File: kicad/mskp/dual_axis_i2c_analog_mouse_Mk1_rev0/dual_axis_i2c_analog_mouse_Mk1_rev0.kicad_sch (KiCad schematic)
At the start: 16 parts, among them J1 I2C_input_controller_JST, J2 I2C_input_controller_pads, J3 mouse_input_pads, J4 mouse_input_JST, U1 ADS1113IDGS, U2 AMS1117-3.3

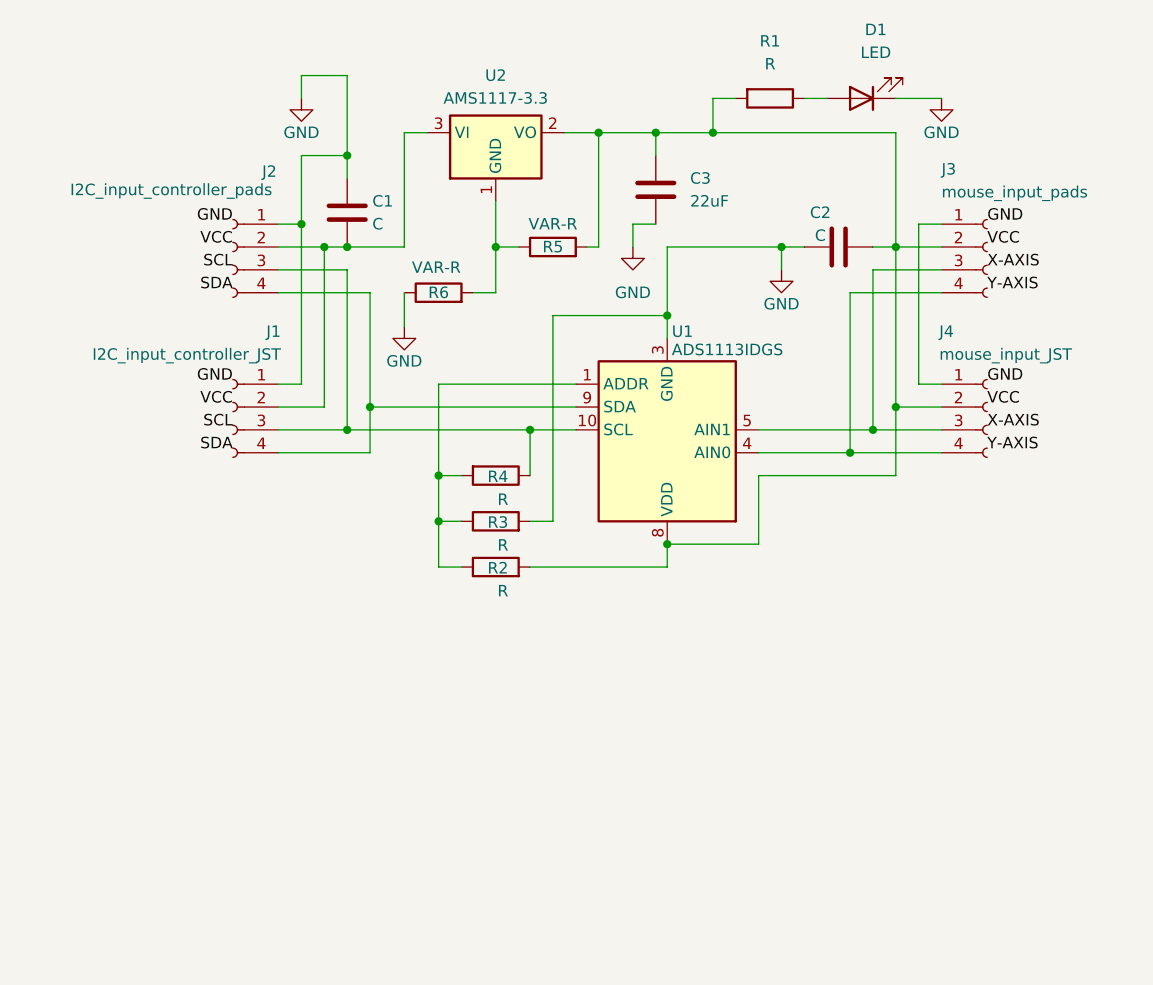
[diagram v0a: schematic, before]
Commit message: Further refinement of first drafts adding specific components
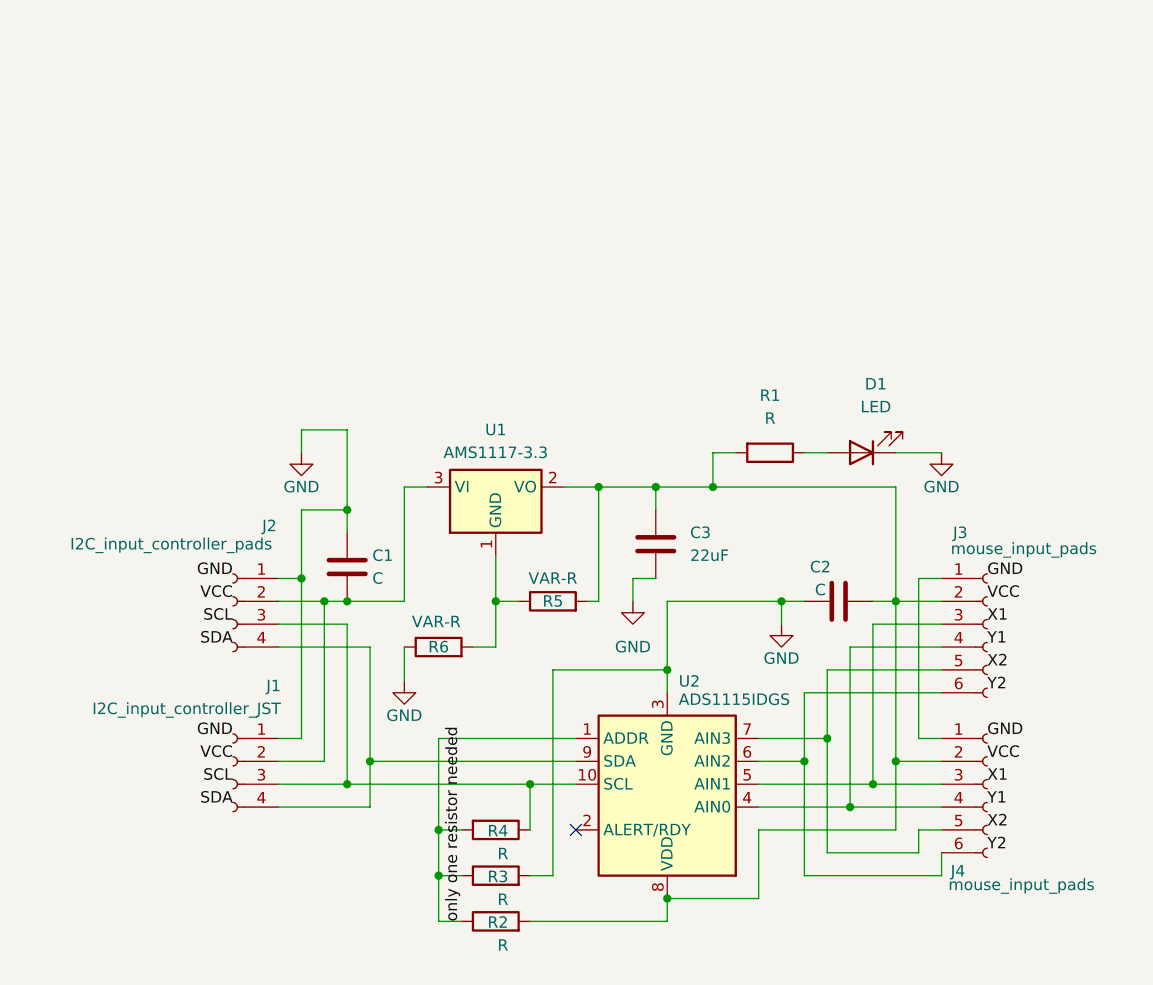
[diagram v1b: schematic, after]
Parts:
- removed J3: mouse_input_pads, symbol Connector:Conn_01x04_Socket
- removed J4: mouse_input_JST, symbol Connector:Conn_01x04_Socket
- removed U1: ADS1113IDGS, Package_SO:TSSOP-10_3x3mm_P0.5mm, symbol Analog_ADC:ADS1113IDGS
- added J3, J4: mouse_input_pads, symbol Connector:Conn_01x06_Socket
- added U2: ADS1115IDGS, Package_SO:TSSOP-10_3x3mm_P0.5mm, symbol Analog_ADC:ADS1115IDGS
- renumbered U2 to U1
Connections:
- net GND: now also U2.3 (GND)
- net at C2.2, C3.1, R1.2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: now also J3.2 (Pin_2), J4.2 (Pin_2), U2.8 (VDD)
- net only one resistor needed: now reaches R2.1, R3.1, R4.2
- net only one resistor needed: now also U2.1 (ADDR)
- net at J1.3 (Pin_3), J2.3 (Pin_3), R4.1: now also U2.10 (SCL)
- net at J1.4 (Pin_4), J2.4 (Pin_4): now also U2.9 (SDA)
- new net: J3.1 (Pin_1), J4.1 (Pin_1)
- new net: J3.3 (Pin_3), J4.3 (Pin_3), U2.5 (AIN1)
- new net: J3.4 (Pin_4), J4.4 (Pin_4), U2.4 (AIN0)
- new net: J3.5 (Pin_5), J4.5 (Pin_5), U2.7 (AIN3)
- new net: J3.6 (Pin_6), J4.6 (Pin_6), U2.6 (AIN2)
- no-connect marks 0 -> 1
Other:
- moved on the sheet: C1, C2, C3, D1, J1, J2, R1, R2, R3, R4, R5, R6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

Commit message: Initital footprint assignment to all control boards
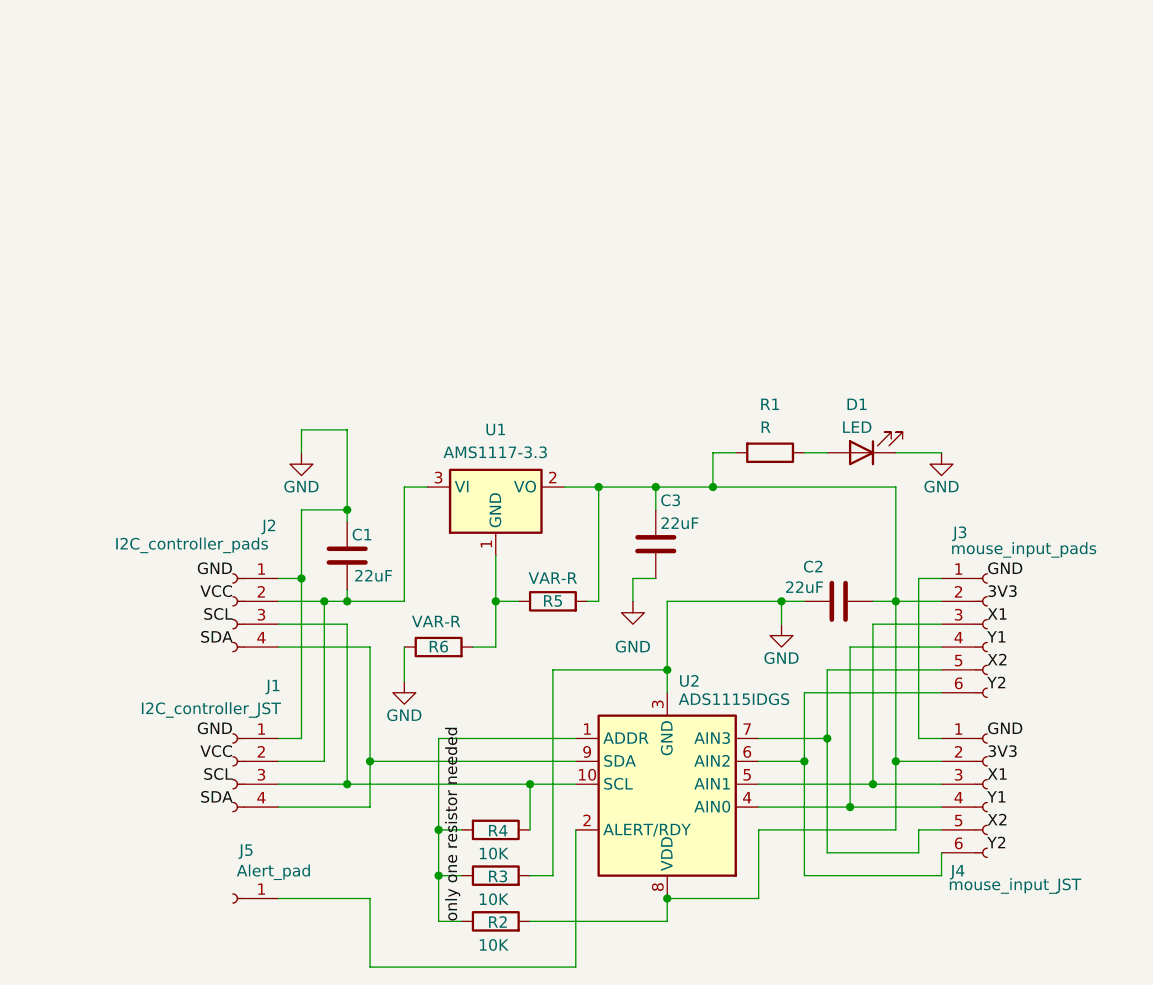
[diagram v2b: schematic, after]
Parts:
- added J5: Alert_pad, Connector_PinSocket_2.54mm:PinSocket_1x01_P2.54mm_Vertical, symbol Connector:Conn_01x01_Socket
- C1, C2: value C -> 22uF; footprint (none) -> Capacitor_SMD:C_1206_3216Metric_Pad1.33x1.80mm_HandSolder
- C3: footprint (none) -> Capacitor_SMD:C_1206_3216Metric_Pad1.33x1.80mm_HandSolder
- D1: footprint (none) -> LED_SMD:LED_0805_2012Metric_Pad1.15x1.40mm_HandSolder
- J1: value I2C_input_controller_JST -> I2C_controller_JST; footprint (none) -> Connector_JST:JST_GH_SM04B-GHS-TB_1x04-1MP_P1.25mm_Horizontal
- J2: value I2C_input_controller_pads -> I2C_controller_pads; footprint (none) -> Connector_PinSocket_2.54mm:PinSocket_1x04_P2.54mm_Vertical
- J3: footprint (none) -> Connector_PinSocket_2.54mm:PinSocket_1x06_P2.54mm_Vertical
- J4: value mouse_input_pads -> mouse_input_JST; footprint (none) -> Connector_JST:JST_GH_SM06B-GHS-TB_1x06-1MP_P1.25mm_Horizontal
- R1, R5, R6: footprint (none) -> Resistor_THT:R_Axial_DIN0207_L6.3mm_D2.5mm_P7.62mm_Horizontal
- R2, R3, R4: value R -> 10K; footprint (none) -> Resistor_THT:R_Axial_DIN0207_L6.3mm_D2.5mm_P7.62mm_Horizontal
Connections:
- net at U2.2 (ALERT/RDY): now also J5.1 (Pin_1)
- no-connect marks 1 -> 0
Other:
- moved on the sheet: C1

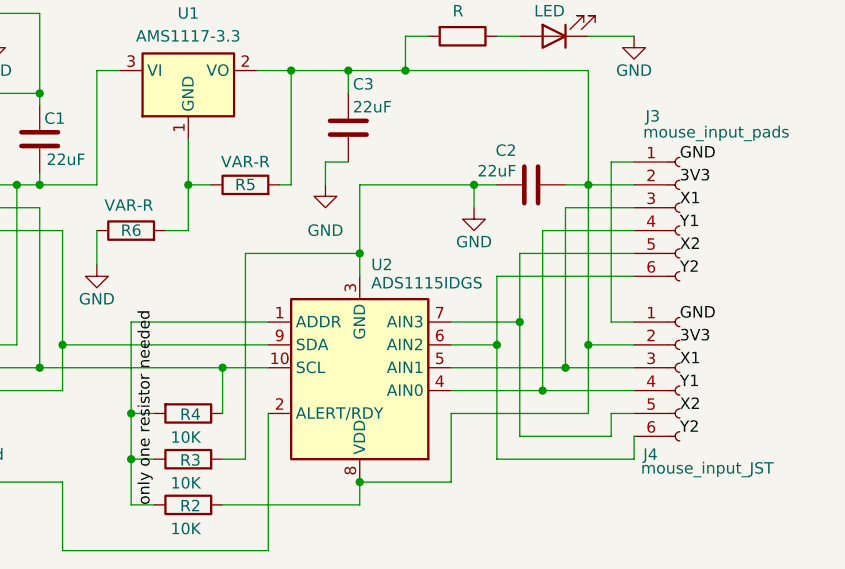
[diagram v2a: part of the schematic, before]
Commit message: Initial layout of dual_axis_i2c_analog_mouse_Mk1_rev0 PCB traces
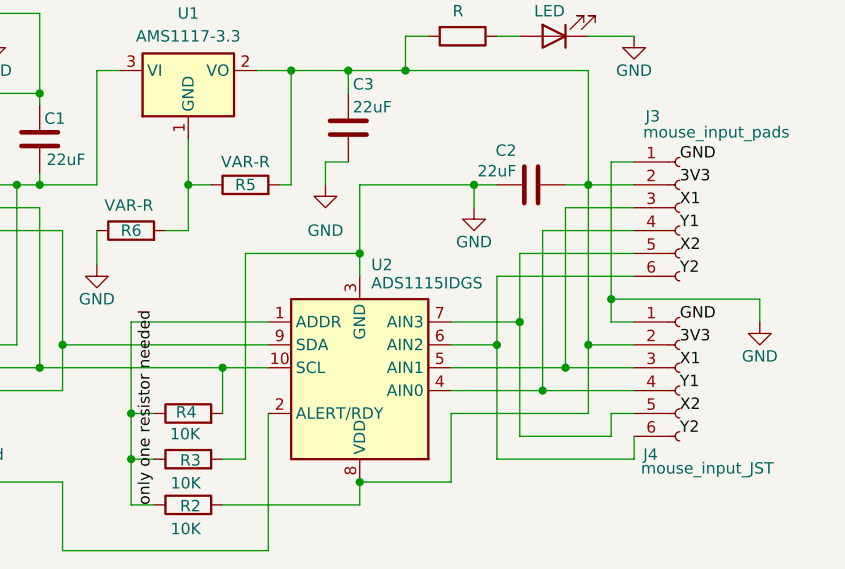
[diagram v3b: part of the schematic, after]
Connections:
- net GND: now also J3.1 (Pin_1), J4.1 (Pin_1)
- net only one resistor needed: now also R4.1; no longer R4.2
- net at J1.3 (Pin_3), J2.3 (Pin_3), U2.10 (SCL): now also R4.2; no longer R4.1
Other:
- moved on the sheet: R4
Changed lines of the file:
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@@
+	)
+	(junction
+		(at 184.15 99.06)
+		(diameter 0)
+		(color 0 0 0 0)
 	)
 	(junction
@@
 	(wire
 		(pts
-			(xy 184.15 83.82) (xy 184.15 101.6)
+			(xy 184.15 83.82) (xy 184.15 99.06)
 		)
 		(stroke
@@
 	(wire
 		(pts
+			(xy 184.15 99.06) (xy 184.15 101.6)
+		)
+		(stroke
+			(width 0)
+			(type default)
+		)
+	)
+	(wire
+		(pts
 			(xy 140.97 106.68) (xy 140.97 111.76)
 		)
@@
 	(wire
 		(pts
+			(xy 184.15 99.06) (xy 200.66 99.06)
+		)
+		(stroke
+			(width 0)
+			(type default)
+		)
+	)
+	(wire
+		(pts
 			(xy 113.03 86.36) (xy 118.11 86.36)
 		)
@@
 		(pts
 			(xy 166.37 101.6) (xy 173.99 101.6)
+		)
+		(stroke
+			(width 0)
+			(type default)
+		)
+	)
+	(wire
+		(pts
+			(xy 200.66 99.06) (xy 200.66 101.6)
 		)
 		(stroke
@@
 	)
 	(symbol
+		(lib_id "power:GND")
+		(at 200.66 101.6 0)
+		(mirror y)
+		(unit 1)
+		(exclude_from_sim no)
+		(in_bom yes)
+		(on_board yes)
+		(dnp no)
+		(property "Reference" "#PWR06"
+			(at 200.66 107.95 0)
+			(effects
+				(font
+					(size 1.27 1.27)
+				)
+				(hide yes)
+			)
+		)
+		(property "Value" "GND"
+			(at 200.66 105.41 0)
+			(effects
+				(font
+					(size 1.27 1.27)
+				)
+			)
+		)
+		(property "Footprint" ""
+			(at 200.66 101.6 0)
+			(effects
+				(font
+					(size 1.27 1.27)
+				)
+				(hide yes)
+			)
+		)
+		(property "Datasheet" ""
+			(at 200.66 101.6 0)
+			(effects
+				(font
+					(size 1.27 1.27)
+				)
+				(hide yes)
+			)
+		)
+		(property "Description" "Power symbol creates a global label with name \"GND\" , ground"
+			(at 200.66 101.6 0)
+			(effects
+				(font
+					(size 1.27 1.27)
+				)
+				(hide yes)
+			)
+		)
+		(pin "1"
+		)
+		(instances
+			(project "dual_axis_i2c_analog_mouse_Mk1_rev0"
+				(path "/97f8c77d-fcb8-4f12-a3ba-2ac0f737e7f7"
+					(reference "#PWR06")
+					(unit 1)
+				)
+			)
+		)
+	)
+	(symbol
 		(lib_id "Device:R")
-		(at 137.16 111.76 270)
+		(at 137.16 111.76 90)
 		(unit 1)
 		(exclude_from_sim no)
@@
 		(dnp no)
 		(property "Reference" "R4"
-			(at 138.557 111.887 90)
+			(at 135.763 111.633 90)
 			(effects
 				(font
@@
 		)
 		(property "Value" "10K"
-			(at 138.557 114.427 90)
+			(at 135.128 114.046 90)
 			(effects
 				(font
@@
 		)
 		(property "Footprint" "Resistor_THT:R_Axial_DIN0207_L6.3mm_D2.5mm_P7.62mm_Horizontal"
-			(at 137.16 109.982 90)
-			(effects
-				(font
+			(at 137.16 113.538 90)
+			(effects
+				(font

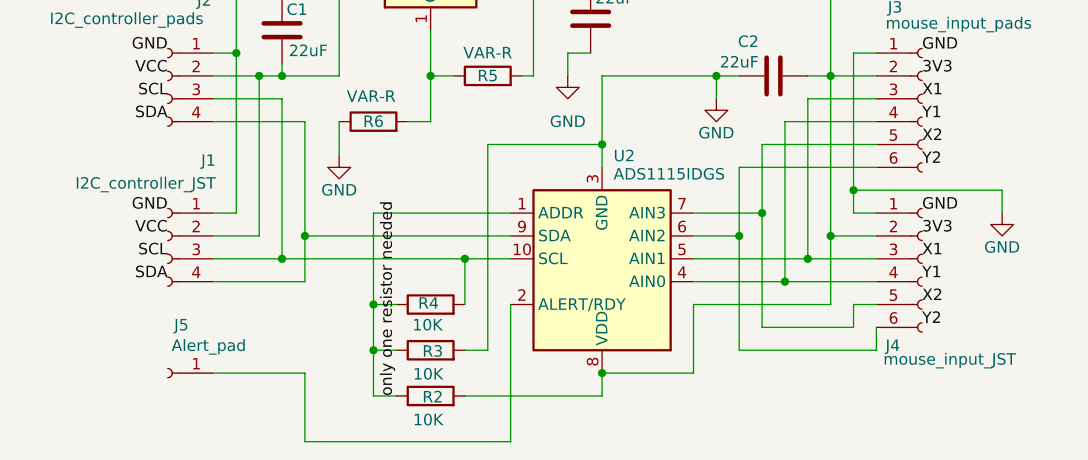
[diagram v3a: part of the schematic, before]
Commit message: Adds silkscreen for dual_axis_i2c_analog_mouse_Mk1_rev0 PCB
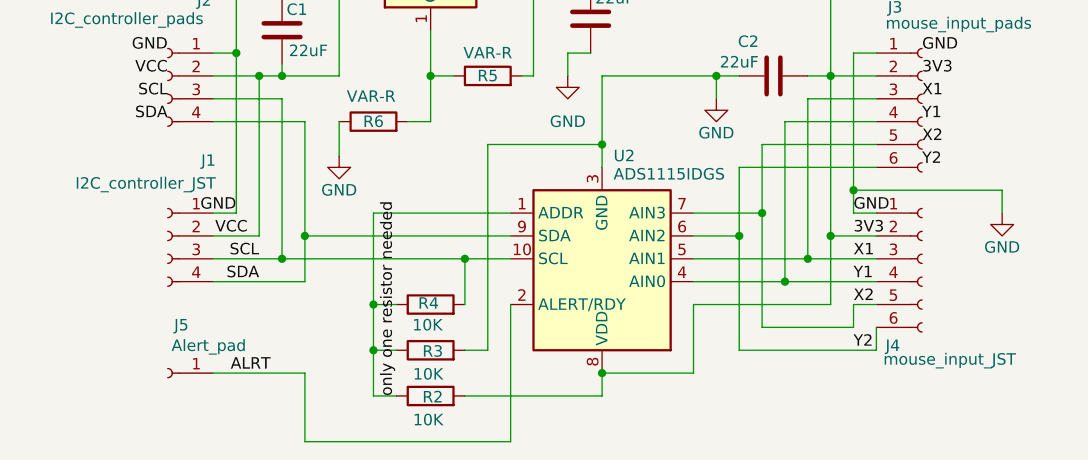
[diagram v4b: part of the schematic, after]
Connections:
- net 3V3: now also C2.2, C3.1, J3.2 (Pin_2), J4.2 (Pin_2), R1.2, R2.2, R5.2, U1.2 (VO), U2.8 (VDD)
- net SCL: now also J1.3 (Pin_3), J2.3 (Pin_3), R4.2, U2.10 (SCL)
- net SDA: now also J1.4 (Pin_4), J2.4 (Pin_4), U2.9 (SDA)
- net VCC: now also C1.2, J1.2 (Pin_2), J2.2 (Pin_2), U1.3 (VI)
- net X1: now also J3.3 (Pin_3), J4.3 (Pin_3), U2.5 (AIN1)
- net X2: now also J3.5 (Pin_5), J4.5 (Pin_5), U2.7 (AIN3)
- net Y1: now also J3.4 (Pin_4), J4.4 (Pin_4), U2.4 (AIN0)
- net Y2: now also J3.6 (Pin_6), J4.6 (Pin_6), U2.6 (AIN2)
- net ALRT: now reaches J5.1 (Pin_1), U2.2 (ALERT/RDY)
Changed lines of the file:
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@@
 	)
 	(label "X2"
-		(at 191.77 111.76 0)
+		(at 184.15 111.76 0)
 		(fields_autoplaced yes)
 		(effects
@@
 	)
 	(label "SCL"
-		(at 107.95 106.68 180)
+		(at 118.11 106.68 180)
 		(fields_autoplaced yes)
 		(effects
@@
 	)
 	(label "SDA"
-		(at 107.95 109.22 180)
+		(at 118.11 109.22 180)
 		(fields_autoplaced yes)
 		(effects
@@
 	)
 	(label "Y1"
-		(at 191.77 109.22 0)
+		(at 184.15 109.22 0)
 		(fields_autoplaced yes)
 		(effects
@@
 	)
 	(label "Y2"
-		(at 191.77 114.3 0)
+		(at 184.15 116.84 0)
 		(fields_autoplaced yes)
 		(effects
@@
 	)
 	(label "VCC"
-		(at 107.95 104.14 180)
+		(at 116.84 104.14 180)
 		(fields_autoplaced yes)
 		(effects
@@
 	)
 	(label "3V3"
-		(at 191.77 104.14 0)
+		(at 184.15 104.14 0)
 		(fields_autoplaced yes)
 		(effects
@@
 		)
 	)
+	(label "ALRT"
+		(at 119.38 119.38 180)
+		(fields_autoplaced yes)
+		(effects
+			(font
+				(size 1.27 1.27)
+			)
+			(justify right bottom)
+		)
+	)
 	(label "VCC"
 		(at 107.95 86.36 180)
@@
 	)
 	(label "GND"
-		(at 191.77 101.6 0)
+		(at 184.15 101.6 0)
 		(fields_autoplaced yes)
 		(effects
@@
 	)
 	(label "X1"
-		(at 191.77 106.68 0)
+		(at 184.15 106.68 0)
 		(fields_autoplaced yes)
 		(effects
@@
 	)
 	(label "GND"
-		(at 107.95 101.6 180)
+		(at 115.57 101.6 180)
 		(fields_autoplaced yes)
 		(effects
